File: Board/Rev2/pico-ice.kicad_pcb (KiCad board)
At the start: 4 copper layers, 22.9 x 61 mm, 99 parts, among them J1 USB_C_Receptacle_USB2.0, J2 Conn_02x20_Odd_Even, J3 Conn_02x20_Odd_Even, J4 PB_SEL, Q1 2N7002, SW1 PTS820 J25K SMTR LFS, SW2 PTS820 J25K SMTR LFS, U1 CL9293A12L5M, U2 W25Q32JVSSIQ, U3 RP2040, U4 CL9293A33L5M, U5 APS6404L-3SQN-SN, U6 ICE40UP5K-SG48ITR, U8 W25Q32JVSSIQ, Y1 12 MHz

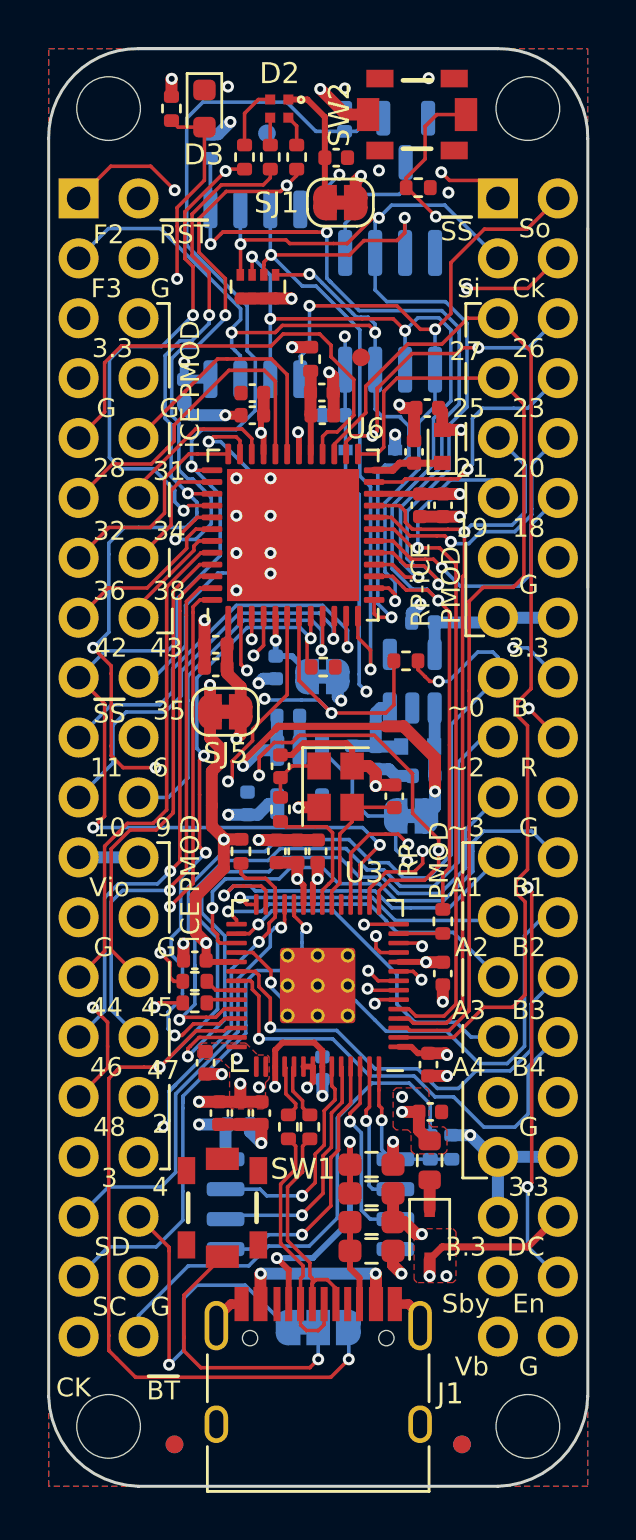
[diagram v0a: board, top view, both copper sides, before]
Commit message: Fixed routing and also some silkscreen DRC's
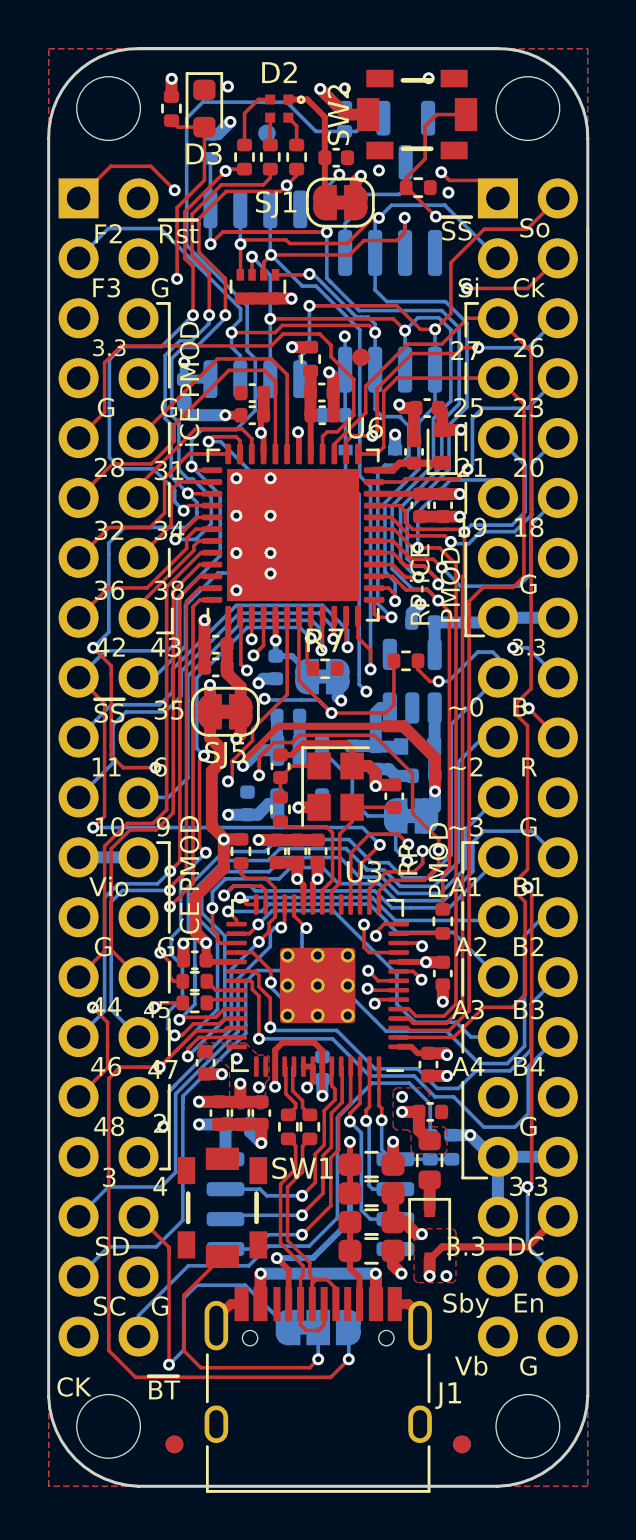
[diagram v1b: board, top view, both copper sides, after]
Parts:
- R7: value 100K -> 10K
- moved R7 0.11 mm to (72.7, 100.0)
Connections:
- U3 pad 11: /ICE_SO -> /ICE_SI
- U3 pad 14: /ICE_SI -> /ICE_SO
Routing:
- net /ICE_SI: track 60.3 -> 61.3 mm
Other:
- board text removed: "~{RST}"

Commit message: Changed version on the board so it reads Rev2
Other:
- board text added: "pico-ice Rev2"
- board text removed: "Vbus"
- board text removed: "pico-ice v2"
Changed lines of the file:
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@@
     (effects (font (size 0.8 0.8) (thickness 0.15)) (justify mirror))
   )
-  (gr_text "Vbus" (at 78.775718 129.929071) (layer "B.SilkS")
+  (gr_text "Vb" (at 79.664718 129.802071) (layer "B.SilkS")
     (effects (font (size 0.8 0.8) (thickness 0.15)) (justify mirror))
   )
@@
     (effects (font (size 0.8 0.8) (thickness 0.15)))
   )
-  (gr_text "pico-ice v2" (at 71.917718 130.056071) (layer "B.Mask")
+  (gr_text "pico-ice Rev2" (at 72.552718 130.310071) (layer "B.Mask")
     (effects (font (size 1.143 1.143) (thickness 0.254)) (justify mirror))
   )

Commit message: Added OSHW logo
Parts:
- added LOGO4: US002140, OSHW_Certification:OSHW_Dual_0.1_Scale_2140, F.Cu at (72.6, 131.8)
